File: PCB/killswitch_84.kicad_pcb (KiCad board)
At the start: 2 copper layers, 25 x 56 mm, 28 parts, among them J1 PWR_IN, J2 BTN/LED, J3 PI, Q1 Q_PMOS_GSD, SW1 SW_Push, U1 ATTINY84-20SSU, U2 TSDP341xx, U3 AZ1117-3.3, U4 TXB0108DQSR

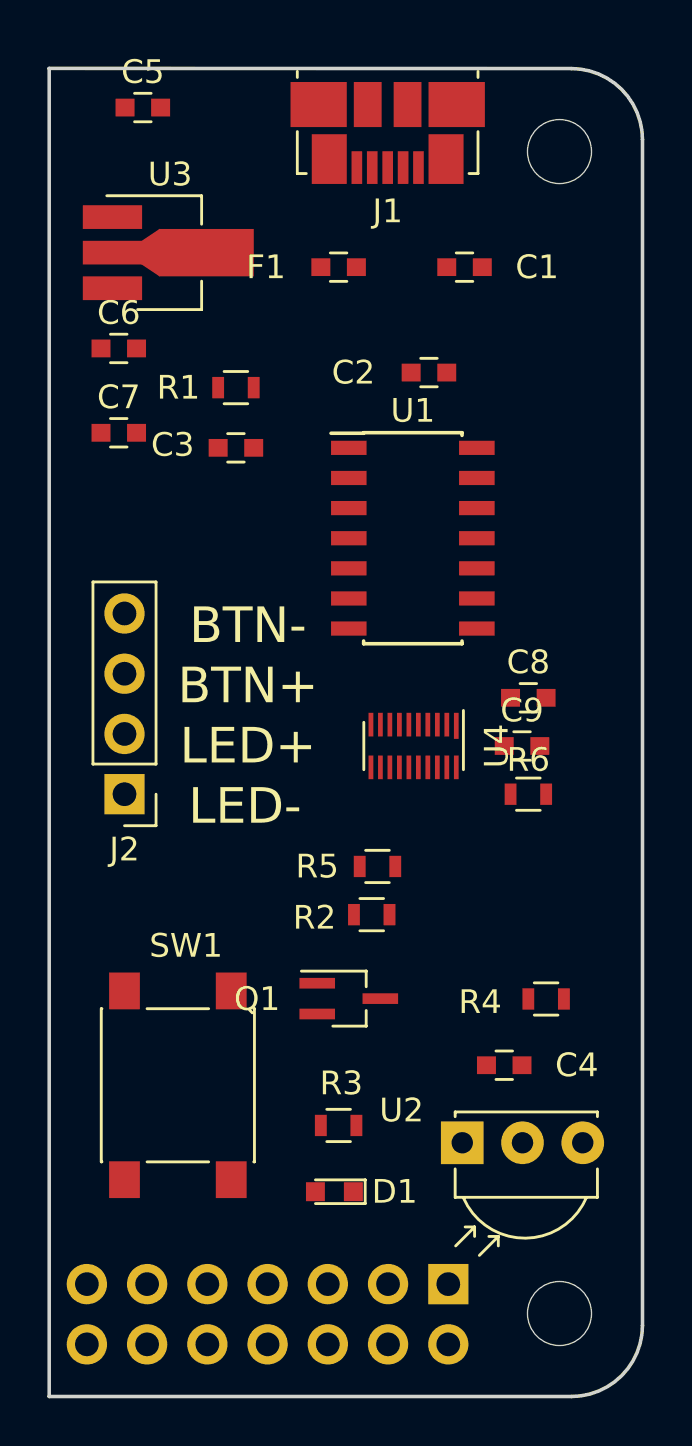
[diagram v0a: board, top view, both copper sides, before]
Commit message: added logo to pcb and sheets
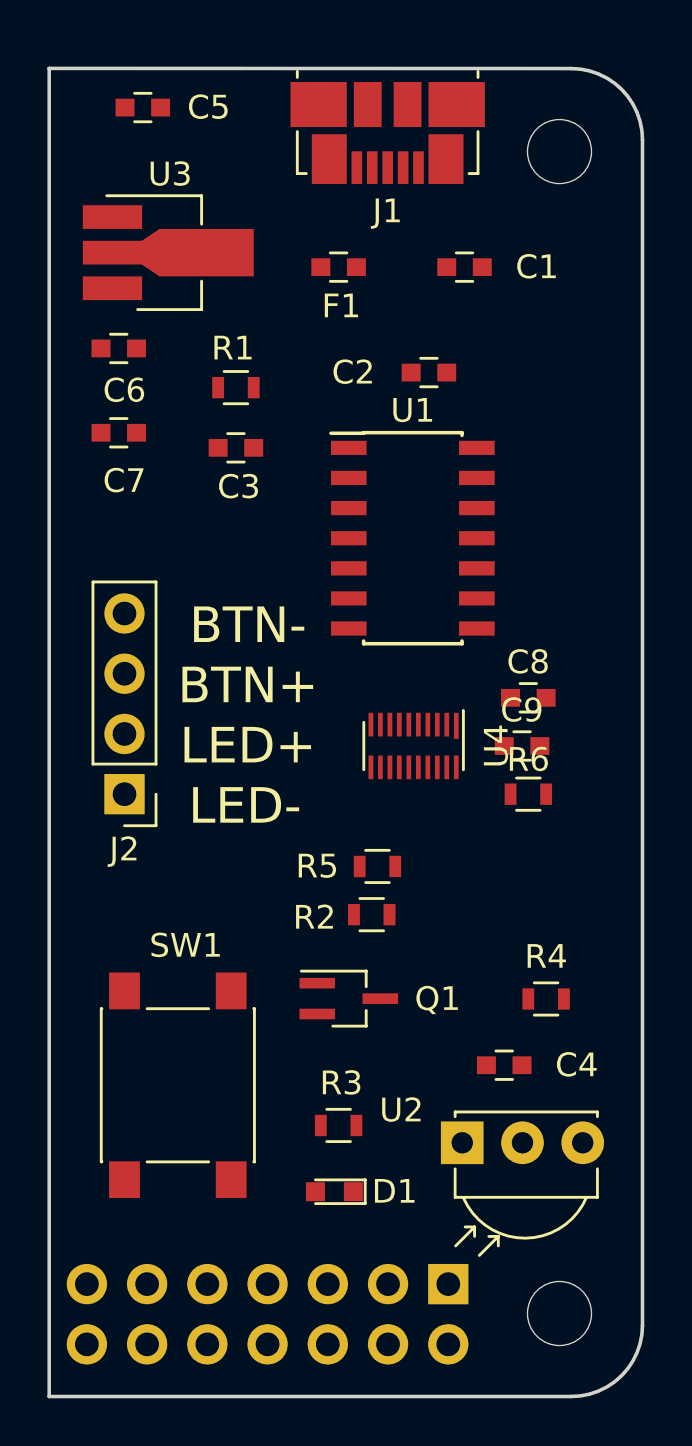
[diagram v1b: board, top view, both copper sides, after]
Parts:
- added ?: , DH_Logo:DH_Logo, B.Cu at (156.7, 82.3)
